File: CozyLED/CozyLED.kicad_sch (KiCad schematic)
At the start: 29 parts, among them J1 Barrel_Jack, J2 LCD DISPLAY, J3 LED Pins, J4 UART, Q1 AO3400A, Q2 AO3400A, Q3 AO3400A, SW1 LEFT, SW2 RIGHT, SW3 EN, SW4 BOOT, U1 ESP32-WROVER-E-N16R8, U2 MAX5033AASA_T

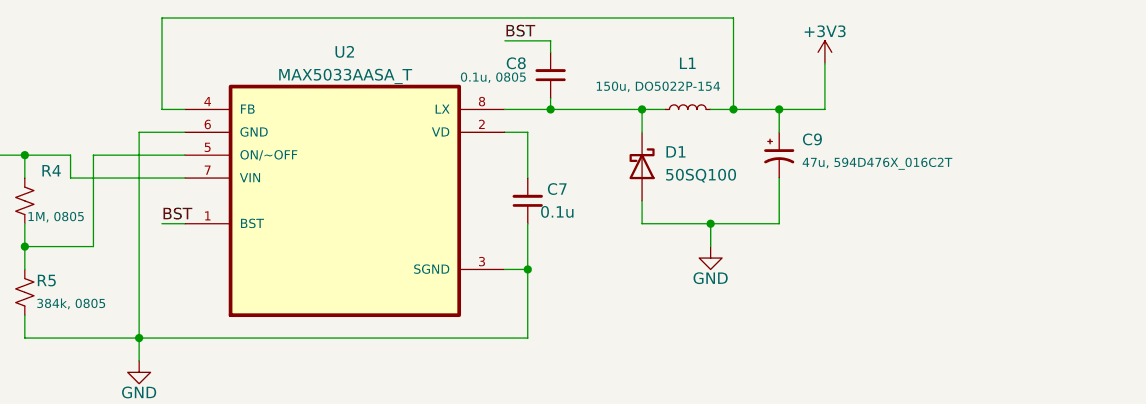
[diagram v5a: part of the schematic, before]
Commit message: Updated CozyLED schematic
Updates
- Added footprints for each component
- Added symbols, footprints, and 3D models for the DC-DC converter's components
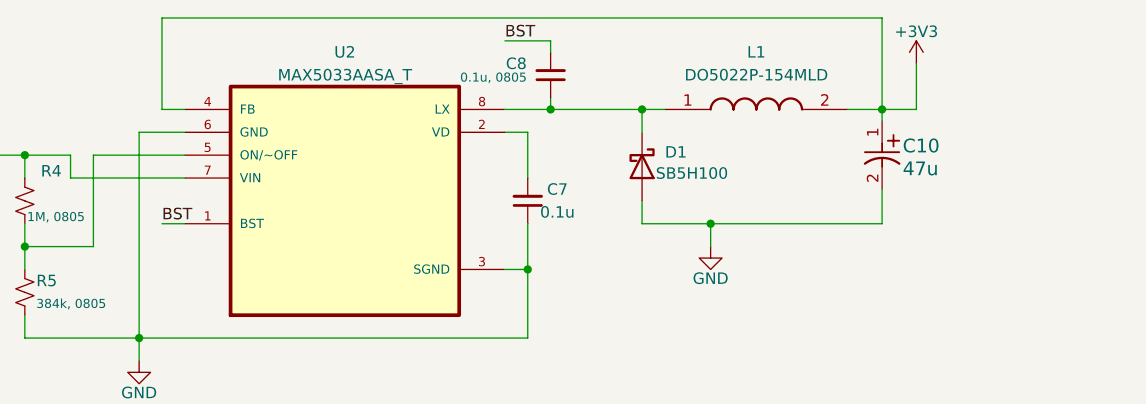
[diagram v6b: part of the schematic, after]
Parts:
- removed C9: 47u, 594D476X_016C2T, symbol Device:C_Polarized_Small_US
- removed L1: 150u, DO5022P-154, symbol Device:L_Small
- added C10: 47u, PCAP_594D_C_VIS, symbol Capacitor:594D476X0016C2T
- added L1: DO5022P-154MLD, DO5022P154MLD, symbol Inductor:DO5022P-154MLD
- C1: footprint (none) -> Capacitor_SMD:C_0603_1608Metric
- C2, C3, C4, C5, C7: footprint (none) -> Capacitor_SMD:C_0402_1005Metric
- C6: footprint (none) -> Capacitor Alum:CAP_EEFK_H13_PAN
- C8: footprint (none) -> Capacitor_SMD:C_0805_2012Metric
- D1: value 50SQ100 -> SB5H100; footprint (none) -> Schottky Diode THT:DIOAD2855W132L835D505
- J2, J3, J4: footprint (none) -> Connector_PinSocket_1.00mm:PinSocket_1x04_P1.00mm_Vertical
- R1, R2, R3: footprint (none) -> Resistor_SMD:R_0603_1608Metric
- R4, R5: footprint (none) -> Resistor_SMD:R_0805_2012Metric
- SW1, SW2: footprint (none) -> Button_Switch_SMD:SW_SPST_TL3305A
- SW3, SW4: footprint (none) -> Button_Switch_SMD:SW_SPST_TS-1088-xR020
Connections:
- net +3V3: now also C10.1, L1.2
- net GND: now also C10.2
- net at C8.1, D1.1 (K), U2.8 (LX): now also L1.1

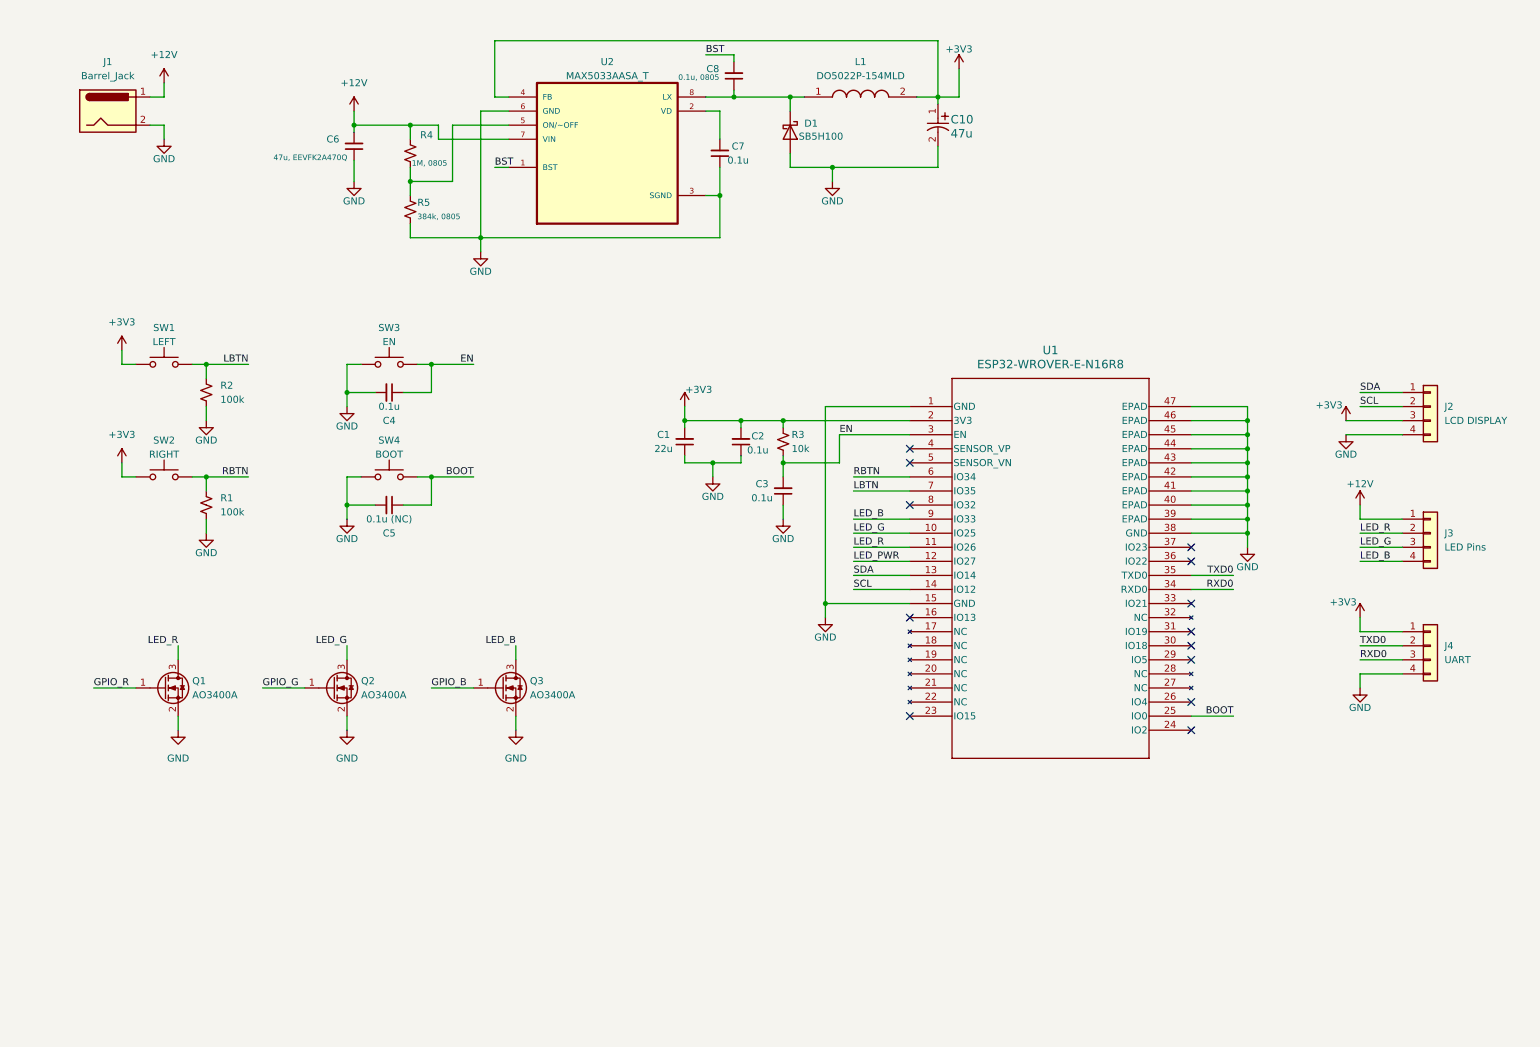
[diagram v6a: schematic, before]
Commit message: Updated CozyLED PCB
Updates:
- Finalized initial revision of schematic (footprints)
- Initial placement of components in layout
- Initial board margins
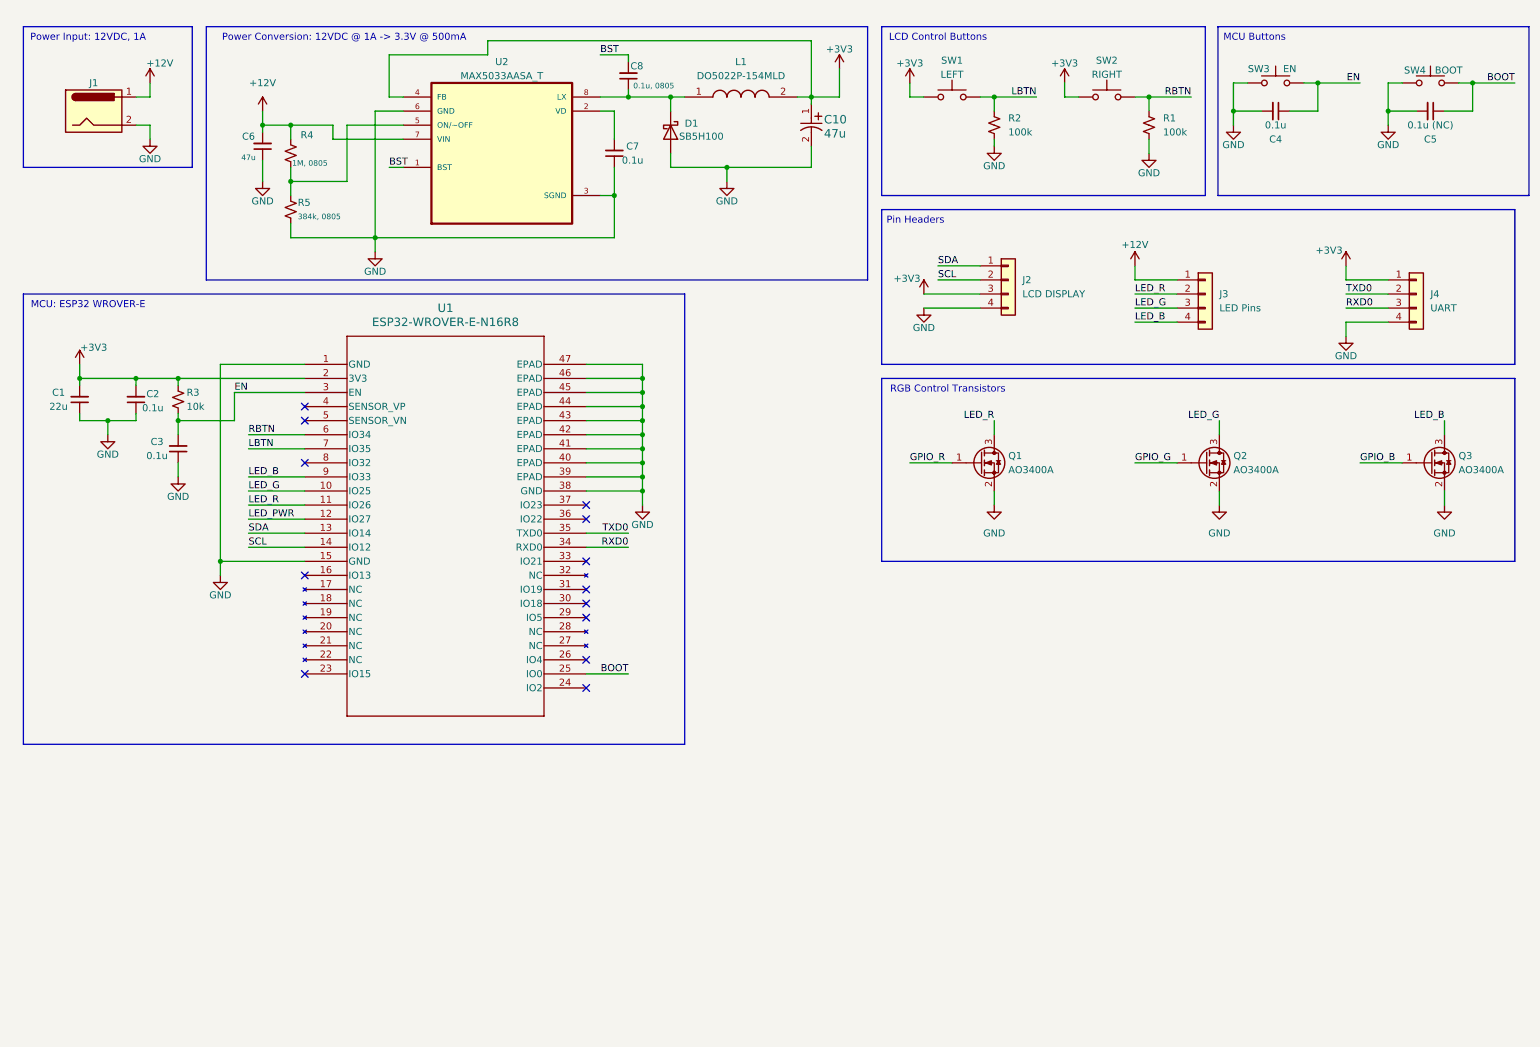
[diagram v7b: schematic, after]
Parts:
- C6: value 47u, EEVFK2A470Q -> 47u
- L1: footprint DO5022P154MLD -> Inductor:DO5022P154MLD
- U1: footprint ESP32-WROVER-E_EXP -> esp:ESP32-WROVER-E_EXP
- U2: footprint MAX5033AASA_T:SOIC127P600X175-8N -> Reg_Switch:SOIC127P600X175-8N
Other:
- note added: "LCD Control Buttons"
- note added: "MCU Buttons"
- note added: "MCU: ESP32 WROVER-E"
- note added: "Pin Headers"
- note added: "Power Conversion: 12VDC @ 1A -> 3.3V @ 500mA"
- note added: "Power Input: 12VDC, 1A"
- note added: "RGB Control Transistors"
- moved on the sheet: C1, C10, C2, C3, C4, C5, C6, C7, C8, D1, J1, J2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

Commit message: Updated CozyLED schematic and PCB
Updates
- Changed version from Rev B to Rev 1.0
- Revised board to be longer and thinner, since it looked ugly as heck
- Added a missing transistor for the power control on the LED output because I'm dumb as shit and forgot to add one
- Added some nice text to the silkscreen so people know what the name is
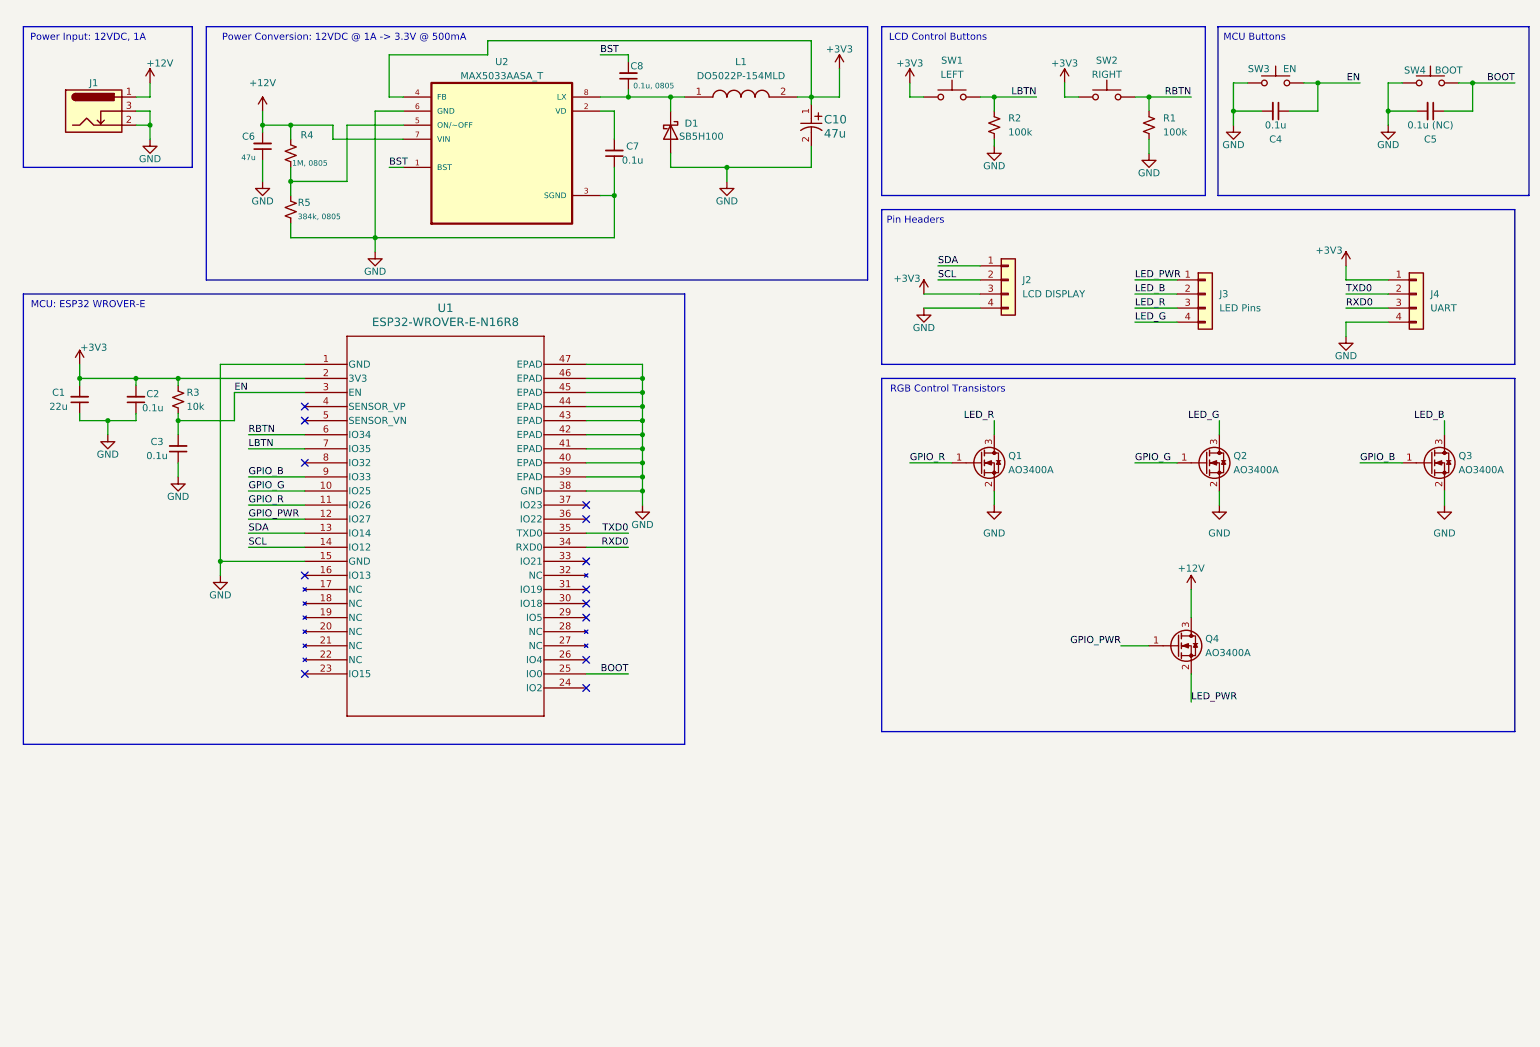
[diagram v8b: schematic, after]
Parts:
- removed J1: Barrel_Jack, Connector_BarrelJack:BarrelJack_SwitchcraftConxall_RAPC10U_Horizontal, symbol Connector:Barrel_Jack
- added J1: Barrel_Jack_Switch, Connector_BarrelJack:BarrelJack_Horizontal, symbol Connector:Barrel_Jack_Switch
- added Q4: AO3400A, Package_TO_SOT_SMD:SOT-23, symbol Transistor_FET:AO3400A
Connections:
- net +12V: now also J1.1, Q4.3 (D); no longer J3.1 (Pin_1)
- net GND: now also J1.2, J1.3
- net GPIO_B: now also U1.9 (IO33)
- net GPIO_G: now also U1.10 (IO25)
- net GPIO_R: now also U1.11 (IO26)
- net LED_B: now also J3.2 (Pin_2); no longer J3.4 (Pin_4), U1.9 (IO33)
- net LED_G: now also J3.4 (Pin_4); no longer J3.3 (Pin_3), U1.10 (IO25)
- net LED_PWR: now also J3.1 (Pin_1), Q4.2 (S); no longer U1.12 (IO27)
- net LED_R: now also J3.3 (Pin_3); no longer J3.2 (Pin_2), U1.11 (IO26)
- new net GPIO_PWR: Q4.1 (G), U1.12 (IO27)
